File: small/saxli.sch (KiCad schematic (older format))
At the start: 7 parts, among them J7 Screw_Terminal_01x08, J8 Screw_Terminal_01x08, J9 Screw_Terminal_01x08

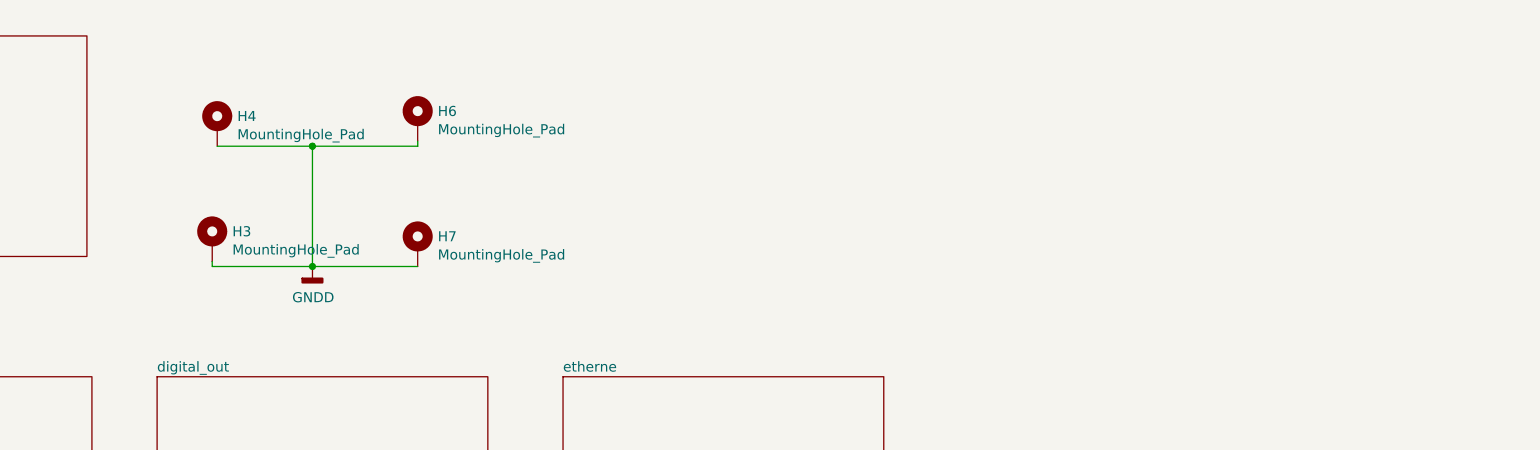
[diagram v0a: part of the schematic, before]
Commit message: sim800 changed to sim808
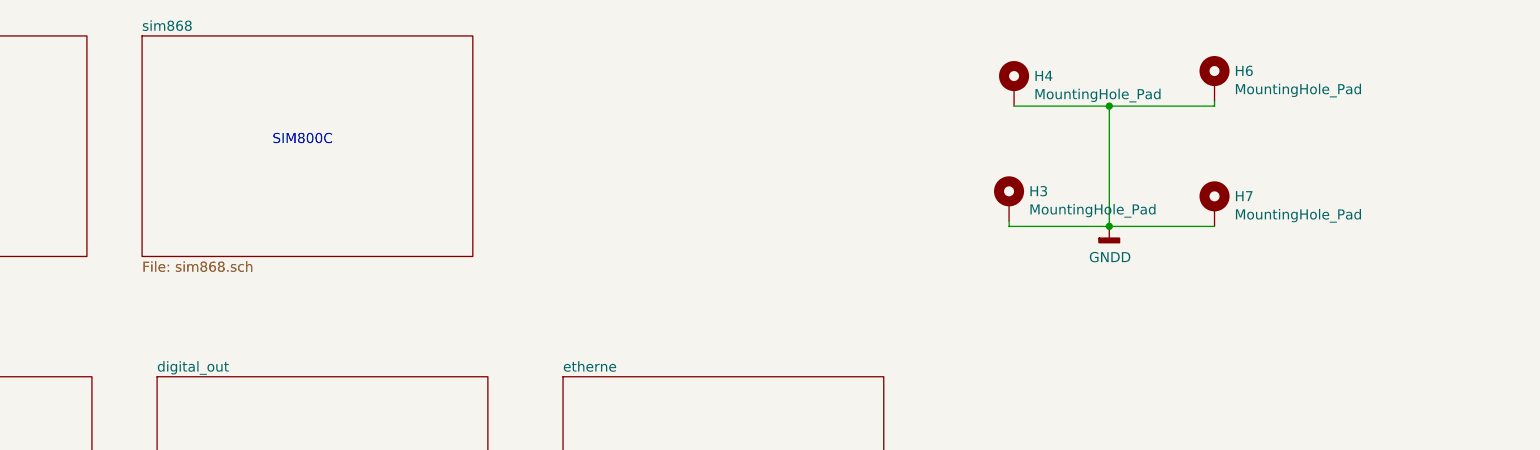
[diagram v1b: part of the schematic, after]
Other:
- note added: "SIM800C\n"
- moved on the sheet: H3, H4, H6, H7
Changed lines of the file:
@@
 $Descr A3 16535 11693
 encoding utf-8
-Sheet 1 8
+Sheet 1 9
 Title ""
 Date ""
@@
 L Mechanical:MountingHole_Pad H4
 U 1 1 5FE64BAA
-P 3200 1525
-F 0 "H4" H 3300 1574 50  0000 L CNN
-F 1 "MountingHole_Pad" H 3300 1483 50  0000 L CNN
-F 2 "MountingHole:MountingHole_3.2mm_M3_Pad" H 3200 1525 50  0001 C CNN
-F 3 "~" H 3200 1525 50  0001 C CNN
-F 4 "#" H 3200 1525 50  0001 C CNN "Mpn"
-	1    3200 1525
+P 7175 1325
+F 0 "H4" H 7275 1374 50  0000 L CNN
+F 1 "MountingHole_Pad" H 7275 1283 50  0000 L CNN
+F 2 "MountingHole:MountingHole_3.2mm_M3_Pad" H 7175 1325 50  0001 C CNN
+F 3 "~" H 7175 1325 50  0001 C CNN
+F 4 "#" H 7175 1325 50  0001 C CNN "Mpn"
+	1    7175 1325
 	1    0    0    -1
 $EndComp
@@
 L Mechanical:MountingHole_Pad H6
 U 1 1 5FE653E8
-P 4200 1500
-F 0 "H6" H 4300 1549 50  0000 L CNN
-F 1 "MountingHole_Pad" H 4300 1458 50  0000 L CNN
-F 2 "MountingHole:MountingHole_3.2mm_M3_Pad" H 4200 1500 50  0001 C CNN
-F 3 "~" H 4200 1500 50  0001 C CNN
-F 4 "#" H 4200 1500 50  0001 C CNN "Mpn"
-	1    4200 1500
+P 8175 1300
+F 0 "H6" H 8275 1349 50  0000 L CNN
+F 1 "MountingHole_Pad" H 8275 1258 50  0000 L CNN
+F 2 "MountingHole:MountingHole_3.2mm_M3_Pad" H 8175 1300 50  0001 C CNN
+F 3 "~" H 8175 1300 50  0001 C CNN
+F 4 "#" H 8175 1300 50  0001 C CNN "Mpn"
+	1    8175 1300
 	1    0    0    -1
 $EndComp
@@
 L Mechanical:MountingHole_Pad H3
 U 1 1 5FE65E3E
-P 3175 2100
-F 0 "H3" H 3275 2149 50  0000 L CNN
-F 1 "MountingHole_Pad" H 3275 2058 50  0000 L CNN
-F 2 "MountingHole:MountingHole_3.2mm_M3_Pad" H 3175 2100 50  0001 C CNN
-F 3 "~" H 3175 2100 50  0001 C CNN
-F 4 "#" H 3175 2100 50  0001 C CNN "Mpn"
-	1    3175 2100
+P 7150 1900
+F 0 "H3" H 7250 1949 50  0000 L CNN
+F 1 "MountingHole_Pad" H 7250 1858 50  0000 L CNN
+F 2 "MountingHole:MountingHole_3.2mm_M3_Pad" H 7150 1900 50  0001 C CNN
+F 3 "~" H 7150 1900 50  0001 C CNN
+F 4 "#" H 7150 1900 50  0001 C CNN "Mpn"
+	1    7150 1900
 	1    0    0    -1
 $EndComp
@@
 L Mechanical:MountingHole_Pad H7
 U 1 1 5FE667D5
-P 4200 2125
-F 0 "H7" H 4300 2174 50  0000 L CNN
-F 1 "MountingHole_Pad" H 4300 2083 50  0000 L CNN
-F 2 "MountingHole:MountingHole_3.2mm_M3_Pad" H 4200 2125 50  0001 C CNN
-F 3 "~" H 4200 2125 50  0001 C CNN
-F 4 "#" H 4200 2125 50  0001 C CNN "Mpn"
-	1    4200 2125
-	1    0    0    -1
-$EndComp
-Wire Wire Line
-	3200 1625 3675 1625
-Wire Wire Line
-	4200 1625 4200 1600
-Wire Wire Line
-	4200 2225 3675 2225
-Wire Wire Line
-	3175 2225 3175 2200
-Connection ~ 3675 1625
-Wire Wire Line
-	3675 1625 4200 1625
-Connection ~ 3675 2225
-Wire Wire Line
-	3675 2225 3175 2225
+P 8175 1925
+F 0 "H7" H 8275 1974 50  0000 L CNN
+F 1 "MountingHole_Pad" H 8275 1883 50  0000 L CNN
+F 2 "MountingHole:MountingHole_3.2mm_M3_Pad" H 8175 1925 50  0001 C CNN
+F 3 "~" H 8175 1925 50  0001 C CNN
+F 4 "#" H 8175 1925 50  0001 C CNN "Mpn"
+	1    8175 1925
+	1    0    0    -1
+$EndComp
+Wire Wire Line
+	7175 1425 7650 1425
+Wire Wire Line
+	8175 1425 8175 1400
+Wire Wire Line
+	8175 2025 7650 2025
+Wire Wire Line
+	7150 2025 7150 2000
+Connection ~ 7650 1425
+Wire Wire Line
+	7650 1425 8175 1425
+Connection ~ 7650 2025
+Wire Wire Line
+	7650 2025 7150 2025
 $Comp
 L power:GNDD #PWR020
 U 1 1 5FEA6B3E
-P 3675 2225
-F 0 "#PWR020" H 3675 1975 50  0001 C CNN
-F 1 "GNDD" H 3679 2070 50  0000 C CNN
-F 2 "" H 3675 2225 50  0001 C CNN
-F 3 "" H 3675 2225 50  0001 C CNN
-	1    3675 2225
-	1    0    0    -1
-$EndComp
-Wire Wire Line
-	3675 1625 3675 2225
+P 7650 2025
+F 0 "#PWR020" H 7650 1775 50  0001 C CNN
+F 1 "GNDD" H 7654 1870 50  0000 C CNN
+F 2 "" H 7650 2025 50  0001 C CNN
+F 3 "" H 7650 2025 50  0001 C CNN
+	1    7650 2025
+	1    0    0    -1
+$EndComp
+Wire Wire Line
+	7650 1425 7650 2025
 Wire Wire Line
 	16125 9525 16125 9500
@@
 Text GLabel 10250 4575 0    50   Input ~ 0
 5V
+$Sheet
+S 2825 1075 1650 1100
+U 602125D9
+F0 "sim868" 50
+F1 "sim868.sch" 50
+$EndSheet
+Text Notes 3475 1625 0    50   ~ 0
+SIM800C\n
 $EndSCHEMATC

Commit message: connector rotated.
added rs485 output.

TODO: add bluetooth port.
check all parts
preaper bom list
prepare mouser list
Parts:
- added R54: 10k, Resistor_SMD:R_0603_1608Metric, symbol Device:R
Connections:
- net labels added: 485_A, 485_B
- net labels removed: GNDPWR
- wire segments 9 -> 10
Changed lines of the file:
@@
 Wire Wire Line
 	7650 2025 7150 2025
-$Comp
-L power:GNDD #PWR020
-U 1 1 5FEA6B3E
-P 7650 2025
-F 0 "#PWR020" H 7650 1775 50  0001 C CNN
-F 1 "GNDD" H 7654 1870 50  0000 C CNN
-F 2 "" H 7650 2025 50  0001 C CNN
-F 3 "" H 7650 2025 50  0001 C CNN
-	1    7650 2025
-	1    0    0    -1
-$EndComp
 Wire Wire Line
 	7650 1425 7650 2025
@@
 Text GLabel 10300 3000 0    50   Input ~ 0
 IS_OUT_1
+Text GLabel 10250 4000 0    50   Input ~ 0
+AN_IN0
+Text GLabel 10250 4100 0    50   Input ~ 0
+AN_IN1
+Text GLabel 10300 2400 0    50   Input ~ 0
+12V
+Text GLabel 10250 3500 0    50   Input ~ 0
+12V
+Text GLabel 10250 4675 0    50   Input ~ 0
+IS_IN0
+Text GLabel 10250 4775 0    50   Input ~ 0
+IS_IN1
+Text GLabel 10250 4475 0    50   Input ~ 0
+12V
+Text GLabel 10250 4575 0    50   Input ~ 0
+5V
+$Sheet
+S 2825 1075 1650 1100
+U 602125D9
+F0 "sim868" 50
+F1 "sim868.sch" 50
+$EndSheet
+Text Notes 3475 1625 0    50   ~ 0
+SIM800C\n
+Text GLabel 10250 4975 0    50   Input ~ 0
+485_A
+Text GLabel 10250 5075 0    50   Input ~ 0
+485_B
+$Comp
+L power:GNDD #PWR0118
+U 1 1 606F157F
+P 10250 4200
+F 0 "#PWR0118" H 10250 3950 50  0001 C CNN
+F 1 "GNDD" V 10254 4090 50  0000 R CNN
+F 2 "" H 10250 4200 50  0001 C CNN
+F 3 "" H 10250 4200 50  0001 C CNN
+	1    10250 4200
+	0    1    1    0
+$EndComp
+$Comp
+L power:GNDD #PWR0120
+U 1 1 606F1E5E
+P 10300 2900
+F 0 "#PWR0120" H 10300 2650 50  0001 C CNN
+F 1 "GNDD" V 10304 2790 50  0000 R CNN
+F 2 "" H 10300 2900 50  0001 C CNN
+F 3 "" H 10300 2900 50  0001 C CNN
+	1    10300 2900
+	0    1    1    0
+$EndComp
 $Comp
 L Connector:Screw_Terminal_01x08 J?
@@
 	1    0    0    -1
 $EndComp
-Text GLabel 10250 4000 0    50   Input ~ 0
-AN_IN0
-Text GLabel 10250 4100 0    50   Input ~ 0
-AN_IN1
-Text GLabel 10300 2400 0    50   Input ~ 0
-12V
-$Comp
-L power:GNDPWR #PWR0118
-U 1 1 60AA1052
-P 10300 2900
-F 0 "#PWR0118" H 10300 2700 50  0001 C CNN
-F 1 "GNDPWR" V 10304 2791 50  0000 R CNN
-F 2 "" H 10300 2850 50  0001 C CNN
-F 3 "" H 10300 2850 50  0001 C CNN
-	1    10300 2900
-	0    1    1    0
-$EndComp
-$Comp
-L power:GNDPWR #PWR0120
-U 1 1 60AA21E2
-P 10250 4200
-F 0 "#PWR0120" H 10250 4000 50  0001 C CNN
-F 1 "GNDPWR" V 10254 4091 50  0000 R CNN
-F 2 "" H 10250 4150 50  0001 C CNN
-F 3 "" H 10250 4150 50  0001 C CNN
-	1    10250 4200
-	0    1    1    0
-$EndComp
-Text GLabel 10250 3500 0    50   Input ~ 0
-12V
+Wire Wire Line
+	10250 5175 9950 5175
+$Comp
+L Device:R R54
+U 1 1 606F480B
+P 9800 5175
+AR Path="/606F480B" Ref="R54"  Part="1"
+AR Path="/6078415F/606F480B" Ref="R?"  Part="1"
+F 0 "R54" V 9593 5175 50  0000 C CNN
+F 1 "10k" V 9684 5175 50  0000 C CNN
+F 2 "Resistor_SMD:R_0603_1608Metric" V 9730 5175 50  0001 C CNN
+F 3 "https://datasheet.lcsc.com/szlcsc/Uniroyal-Elec-0603WAF1002T5E_C25804.pdf" H 9800 5175 50  0001 C CNN
+F 4 "C25804" H 9800 5175 50  0001 C CNN "LCSC"
+F 5 "0.02" H 9800 5175 50  0001 C CNN "Price"
+	1    9800 5175
+	0    1    1    0
+$EndComp
+$Comp
+L power:GNDD #PWR0123
+U 1 1 606F4A26
+P 9650 5175
+F 0 "#PWR0123" H 9650 4925 50  0001 C CNN
+F 1 "GNDD" H 9654 5020 50  0000 C CNN
+F 2 "" H 9650 5175 50  0001 C CNN
+F 3 "" H 9650 5175 50  0001 C CNN
+	1    9650 5175
+	0    1    1    0
+$EndComp
 $Comp
 L Connector:Screw_Terminal_01x08 J?
@@
 	1    0    0    -1
 $EndComp
-Text GLabel 10250 4875 0    50   Input ~ 0
-IS_IN0
-Text GLabel 10250 4975 0    50   Input ~ 0
-IS_IN1
-$Comp
-L power:GNDPWR #PWR0123
-U 1 1 60AD29CA
-P 10250 5175
-F 0 "#PWR0123" H 10250 4975 50  0001 C CNN
-F 1 "GNDPWR" V 10254 5066 50  0000 R CNN
-F 2 "" H 10250 5125 50  0001 C CNN
-F 3 "" H 10250 5125 50  0001 C CNN
-	1    10250 5175
-	0    1    1    0
-$EndComp
-$Comp
-L power:GNDPWR #PWR0124
-U 1 1 60AD2B65
-P 10250 5075
-F 0 "#PWR0124" H 10250 4875 50  0001 C CNN
-F 1 "GNDPWR" V 10254 4966 50  0000 R CNN
-F 2 "" H 10250 5025 50  0001 C CNN
-F 3 "" H 10250 5025 50  0001 C CNN
-	1    10250 5075
-	0    1    1    0
-$EndComp
-Text GLabel 10250 4475 0    50   Input ~ 0
-12V
-Text GLabel 10250 4575 0    50   Input ~ 0
-5V
-$Sheet
-S 2825 1075 1650 1100
-U 602125D9
-F0 "sim868" 50
-F1 "sim868.sch" 50
-$EndSheet
-Text Notes 3475 1625 0    50   ~ 0
-SIM800C\n
+$Comp
+L power:GNDD #PWR020
+U 1 1 5FEA6B3E
+P 10250 4875
+F 0 "#PWR020" H 10250 4625 50  0001 C CNN
+F 1 "GNDD" H 10254 4720 50  0000 C CNN
+F 2 "" H 10250 4875 50  0001 C CNN
+F 3 "" H 10250 4875 50  0001 C CNN
+	1    10250 4875
+	0    1    1    0
+$EndComp
+$Comp
+L power:GNDD #PWR?
+U 1 1 607109EA
+P 7650 2025
+F 0 "#PWR?" H 7650 1775 50  0001 C CNN
+F 1 "GNDD" H 7654 1870 50  0000 C CNN
+F 2 "" H 7650 2025 50  0001 C CNN
+F 3 "" H 7650 2025 50  0001 C CNN
+	1    7650 2025
+	1    0    0    -1
+$EndComp
 $EndSCHEMATC

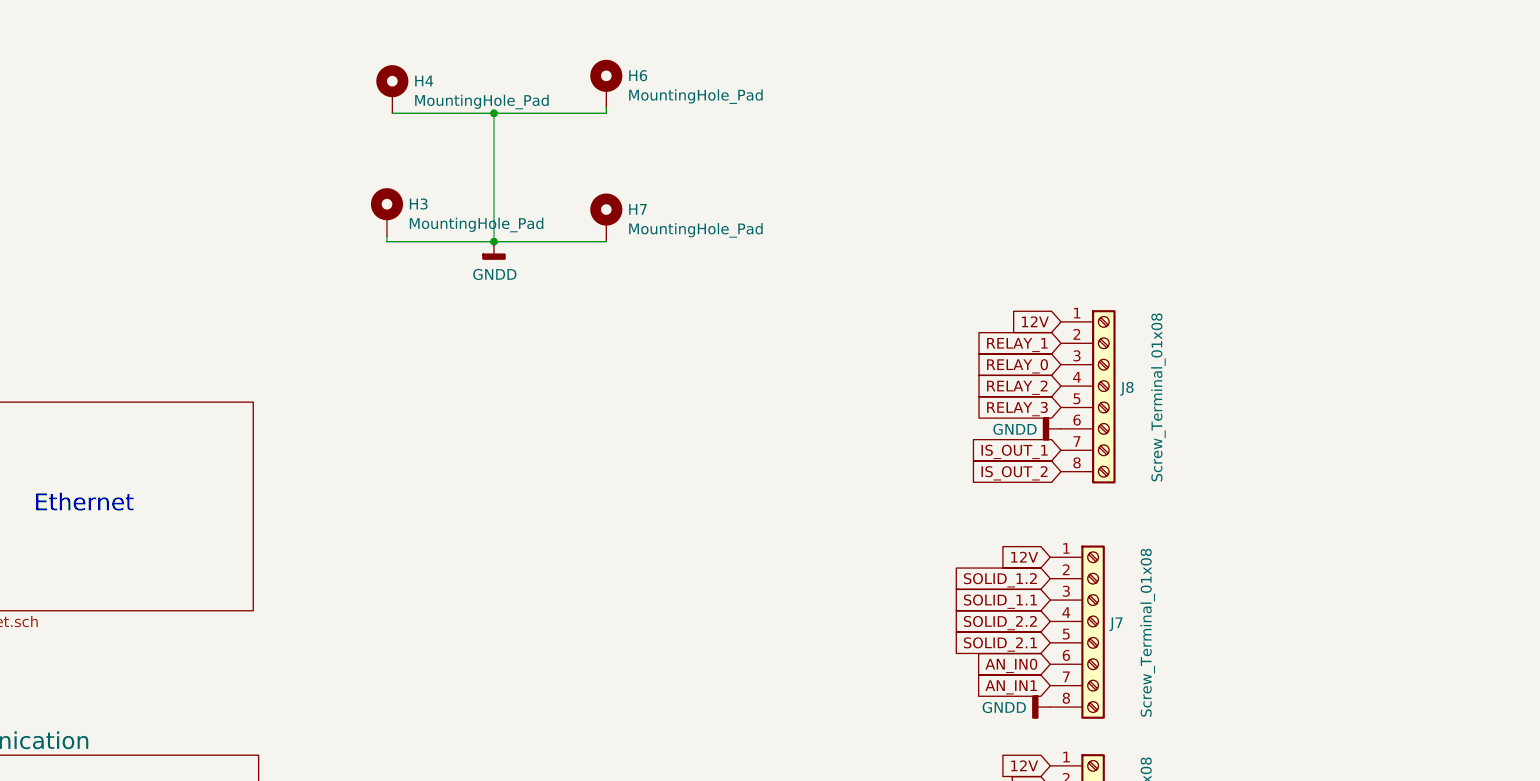
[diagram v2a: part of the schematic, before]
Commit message: GPS connector moved,
antenna matching networks removed

SUPERCAPACITOR from jlpcb used.
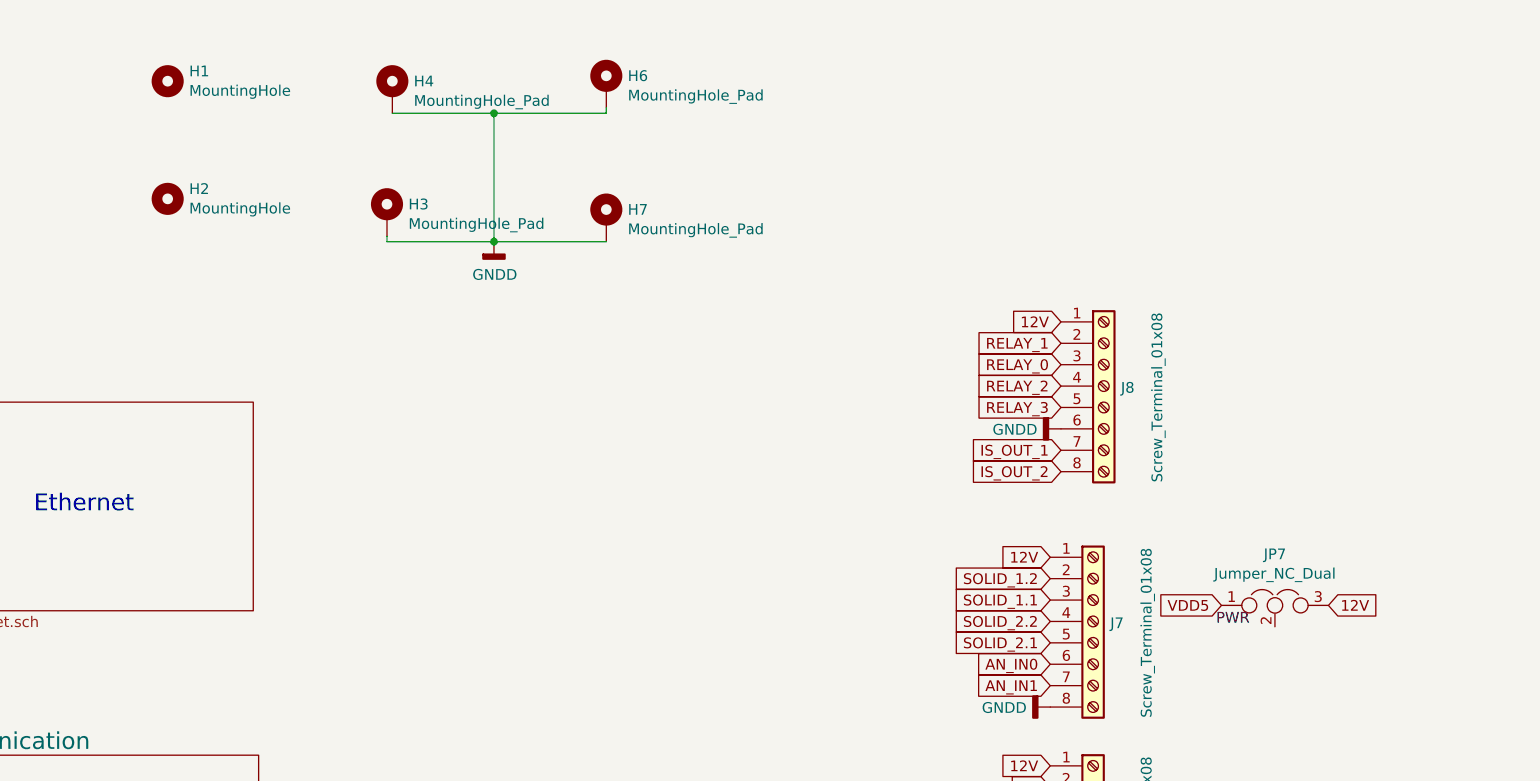
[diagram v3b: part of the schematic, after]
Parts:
- added H1, H2: MountingHole, MountingHole:MountingHole_3.2mm_M3, symbol Mechanical:MountingHole
- added JP7: Jumper_NC_Dual, Jumper:SolderJumper-3_P1.3mm_Open_Pad1.0x1.5mm, symbol Device:Jumper_NC_Dual
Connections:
- net labels added: PWR, VDD5
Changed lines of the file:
@@
 $EndComp
 $Comp
-L power:GNDD #PWR?
+L power:GNDD #PWR0186
 U 1 1 607109EA
 P 7650 2025
-F 0 "#PWR?" H 7650 1775 50  0001 C CNN
+F 0 "#PWR0186" H 7650 1775 50  0001 C CNN
 F 1 "GNDD" H 7654 1870 50  0000 C CNN
 F 2 "" H 7650 2025 50  0001 C CNN
@@
 	1    0    0    -1
 $EndComp
+$Comp
+L Mechanical:MountingHole H1
+U 1 1 6029E07F
+P 6125 1275
+F 0 "H1" H 6225 1321 50  0000 L CNN
+F 1 "MountingHole" H 6225 1230 50  0000 L CNN
+F 2 "MountingHole:MountingHole_3.2mm_M3" H 6125 1275 50  0001 C CNN
+F 3 "~" H 6125 1275 50  0001 C CNN
+	1    6125 1275
+	1    0    0    -1
+$EndComp
+$Comp
+L Mechanical:MountingHole H2
+U 1 1 6029E5C7
+P 6125 1825
+F 0 "H2" H 6225 1871 50  0000 L CNN
+F 1 "MountingHole" H 6225 1780 50  0000 L CNN
+F 2 "MountingHole:MountingHole_3.2mm_M3" H 6125 1825 50  0001 C CNN
+F 3 "~" H 6125 1825 50  0001 C CNN
+	1    6125 1825
+	1    0    0    -1
+$EndComp
+Text Label 11025 3825 0    50   ~ 0
+PWR
+Text GLabel 11050 3725 0    50   Input ~ 0
+VDD5
+Text GLabel 11550 3725 2    50   Input ~ 0
+12V
+$Comp
+L Device:Jumper_NC_Dual JP?
+U 1 1 603CC966
+P 11300 3725
+AR Path="/657E4F8F/603CC966" Ref="JP?"  Part="1"
+AR Path="/603CC966" Ref="JP7"  Part="1"
+F 0 "JP7" H 11300 3964 50  0000 C CNN
+F 1 "Jumper_NC_Dual" H 11300 3873 50  0000 C CNN
+F 2 "Jumper:SolderJumper-3_P1.3mm_Open_Pad1.0x1.5mm" H 11300 3725 50  0001 C CNN
+F 3 "~" H 11300 3725 50  0001 C CNN
+	1    11300 3725
+	1    0    0    -1
+$EndComp

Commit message: BOM updated
Layout changed
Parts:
- R54: MPN (none) -> 0603WAF1002T5E; source (none) -> 0
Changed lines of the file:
@@
 F 4 "C25804" H 9800 5175 50  0001 C CNN "LCSC"
 F 5 "0.02" H 9800 5175 50  0001 C CNN "Price"
+F 6 "0603WAF1002T5E" H 9800 5175 50  0001 C CNN "MPN"
+F 7 "0" H 9800 5175 50  0001 C CNN "source"
 	1    9800 5175
 	0    1    1    0

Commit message: ENC28j60 package changed to soic 28 17.9
TODO: route
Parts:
- H1, H2, H3, H4, H6, H7, J7, J8, J9, JP7: LCSC (none) -> N/A
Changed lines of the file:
@@
 F 3 "~" H 7175 1325 50  0001 C CNN
 F 4 "#" H 7175 1325 50  0001 C CNN "Mpn"
+F 5 "N/A" H 7175 1325 50  0001 C CNN "LCSC"
 	1    7175 1325
 	1    0    0    -1
@@
 F 3 "~" H 8175 1300 50  0001 C CNN
 F 4 "#" H 8175 1300 50  0001 C CNN "Mpn"
+F 5 "N/A" H 8175 1300 50  0001 C CNN "LCSC"
 	1    8175 1300
 	1    0    0    -1
@@
 F 3 "~" H 7150 1900 50  0001 C CNN
 F 4 "#" H 7150 1900 50  0001 C CNN "Mpn"
+F 5 "N/A" H 7150 1900 50  0001 C CNN "LCSC"
 	1    7150 1900
 	1    0    0    -1
@@
 F 3 "~" H 8175 1925 50  0001 C CNN
 F 4 "#" H 8175 1925 50  0001 C CNN "Mpn"
+F 5 "N/A" H 8175 1925 50  0001 C CNN "LCSC"
 	1    8175 1925
 	1    0    0    -1
@@
 F 2 "TerminalBlock_Phoenix:TerminalBlock_Phoenix_MPT-0,5-8-2.54_1x08_P2.54mm_Horizontal" H 10500 2700 50  0001 C CNN
 F 3 "~" H 10500 2700 50  0001 C CNN
+F 4 "N/A" H 10500 2700 50  0001 C CNN "LCSC"
 	1    10500 2700
 	1    0    0    -1
@@
 F 2 "TerminalBlock_Phoenix:TerminalBlock_Phoenix_MPT-0,5-8-2.54_1x08_P2.54mm_Horizontal" H 10450 3800 50  0001 C CNN
 F 3 "~" H 10450 3800 50  0001 C CNN
+F 4 "N/A" H 10450 3800 50  0001 C CNN "LCSC"
 	1    10450 3800
 	1    0    0    -1
@@
 F 2 "TerminalBlock_Phoenix:TerminalBlock_Phoenix_MPT-0,5-8-2.54_1x08_P2.54mm_Horizontal" H 10450 4775 50  0001 C CNN
 F 3 "~" H 10450 4775 50  0001 C CNN
+F 4 "N/A" H 10450 4775 50  0001 C CNN "LCSC"
 	1    10450 4775
 	1    0    0    -1
@@
 F 2 "MountingHole:MountingHole_3.2mm_M3" H 6125 1275 50  0001 C CNN
 F 3 "~" H 6125 1275 50  0001 C CNN
+F 4 "N/A" H 6125 1275 50  0001 C CNN "LCSC"
 	1    6125 1275
 	1    0    0    -1
@@
 F 2 "MountingHole:MountingHole_3.2mm_M3" H 6125 1825 50  0001 C CNN
 F 3 "~" H 6125 1825 50  0001 C CNN
+F 4 "N/A" H 6125 1825 50  0001 C CNN "LCSC"
 	1    6125 1825
 	1    0    0    -1
@@
 F 2 "Jumper:SolderJumper-3_P1.3mm_Open_Pad1.0x1.5mm" H 11300 3725 50  0001 C CNN
 F 3 "~" H 11300 3725 50  0001 C CNN
+F 4 "N/A" H 11300 3725 50  0001 C CNN "LCSC"
 	1    11300 3725
 	1    0    0    -1
